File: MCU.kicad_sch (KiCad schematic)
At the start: 50 parts, among them U1901 ADG1607xCP, U1902 ADG1607xCP, U1903 LP38690SDX-3.3/NOPB, U1904 MSP430FR5969IRGZR, U1905 MSP430FR5969IRGZR, U1906 TCAN4551RGYRQ1

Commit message: wired channel alerts; added schematic for test pbc
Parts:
- removed TP1907, TP1908: ~, TestPoint:TestPoint_Pad_1.0x1.0mm, symbol Connector:TestPoint_Small
- added TP? (x2): ~, TestPoint:TestPoint_Pad_1.0x1.0mm, symbol Connector:TestPoint_Small
- renumbered C1911 to C?, C1904 to C?, C1915 to C?, C1905 to C?, C1909 to C?, C1903 to C?, C1912 to C?, C1901 to C?, C1906 to C?, C1907 to C?, C1914 to C?, C1902 to C?, C1910 to C?, C1913 to C?, R1904 to R?, R1906 to R?, R1901 to R?, R1902 to R?, R1903 to R?, R1908 to R?, R1909 to R?, R1907 to R?, TP1911 to TP?, TP1910 to TP?, TP1913 to TP?, TP1916 to TP?, TP1909 to TP?, TP1901 to TP?, TP1903 to TP?, TP1904 to TP?, TP1920 to TP?, TP1915 to TP?, TP1917 to TP?, TP1905 to TP?, TP1918 to TP?, TP1912 to TP?, TP1902 to TP?, TP1906 to TP?, TP1914 to TP?, U1906 to U?, U1902 to U?, U1905 to U?
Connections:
- net 5V_DCDC_1/VOUT: now also TP?.1
- net Ch_EN_7x: now also U?.3 (P1.2/TA1.1/TA0CLK/COUT/A2/C2); no longer U?.42 (PJ.6/HFXIN)
- net Ch_EN_8x: now also U?.9 (P1.3/TA1.2/UCB0STE/A3/C3); no longer U?.43 (PJ.7/HFXOUT)
- net MCU_3V3: now also TP?.1
- net Ch_AL_9: now reaches U?.1 (P1.0/TA0.1/DMAE0/RTCCLK/A0/C0/VREF-/VEREF-)
- net Ch_AL_1: now reaches U?.12 (PJ.0/TDO/TB0OUTH/SMCLK/SRSCG1/C6)
- net Ch_AL_2: now reaches U?.13 (PJ.1/TDI/TCLK/MCLK/SRSCG0/C7)
- net Ch_AL_3: now reaches U?.14 (PJ.2/TMS/ACLK/SROSCOFF/C8)
- net Ch_AL_4: now reaches U?.15 (PJ.3/TCK/SRCPUOFF/C9)
- net Ch_AL_10: now reaches U?.2 (P1.1/TA0.2/TA1CLK/COUT/A1/C1/VREF+/VEREF+)
- net Ch_AL_5: now reaches U?.45 (PJ.4/LFXIN)
- net Ch_AL_6: now reaches U?.46 (PJ.5/LFXOUT)
- net VMEAS_BATT_1: no longer names the net of U?.17 (S1A)
- net VMEAS_BATT_2: no longer names the net of U?.18 (S2A)
- new net Ch_AL_7: U?.42 (PJ.6/HFXIN)
- new net Ch_AL_8: U?.43 (PJ.7/HFXOUT)
- no-connect marks 2 -> 4

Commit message: reduced number of DCDC converter for PV panels; updated test pcb
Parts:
- gave numbers to parts that had none: 44
- renumbered C1908 to C1808, R1905 to R1805, TP1919 to TP1819, U1901 to U1801, U1903 to U1803, U1904 to U1804
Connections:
- net 5V_DCDC_1/VOUT renamed +5V

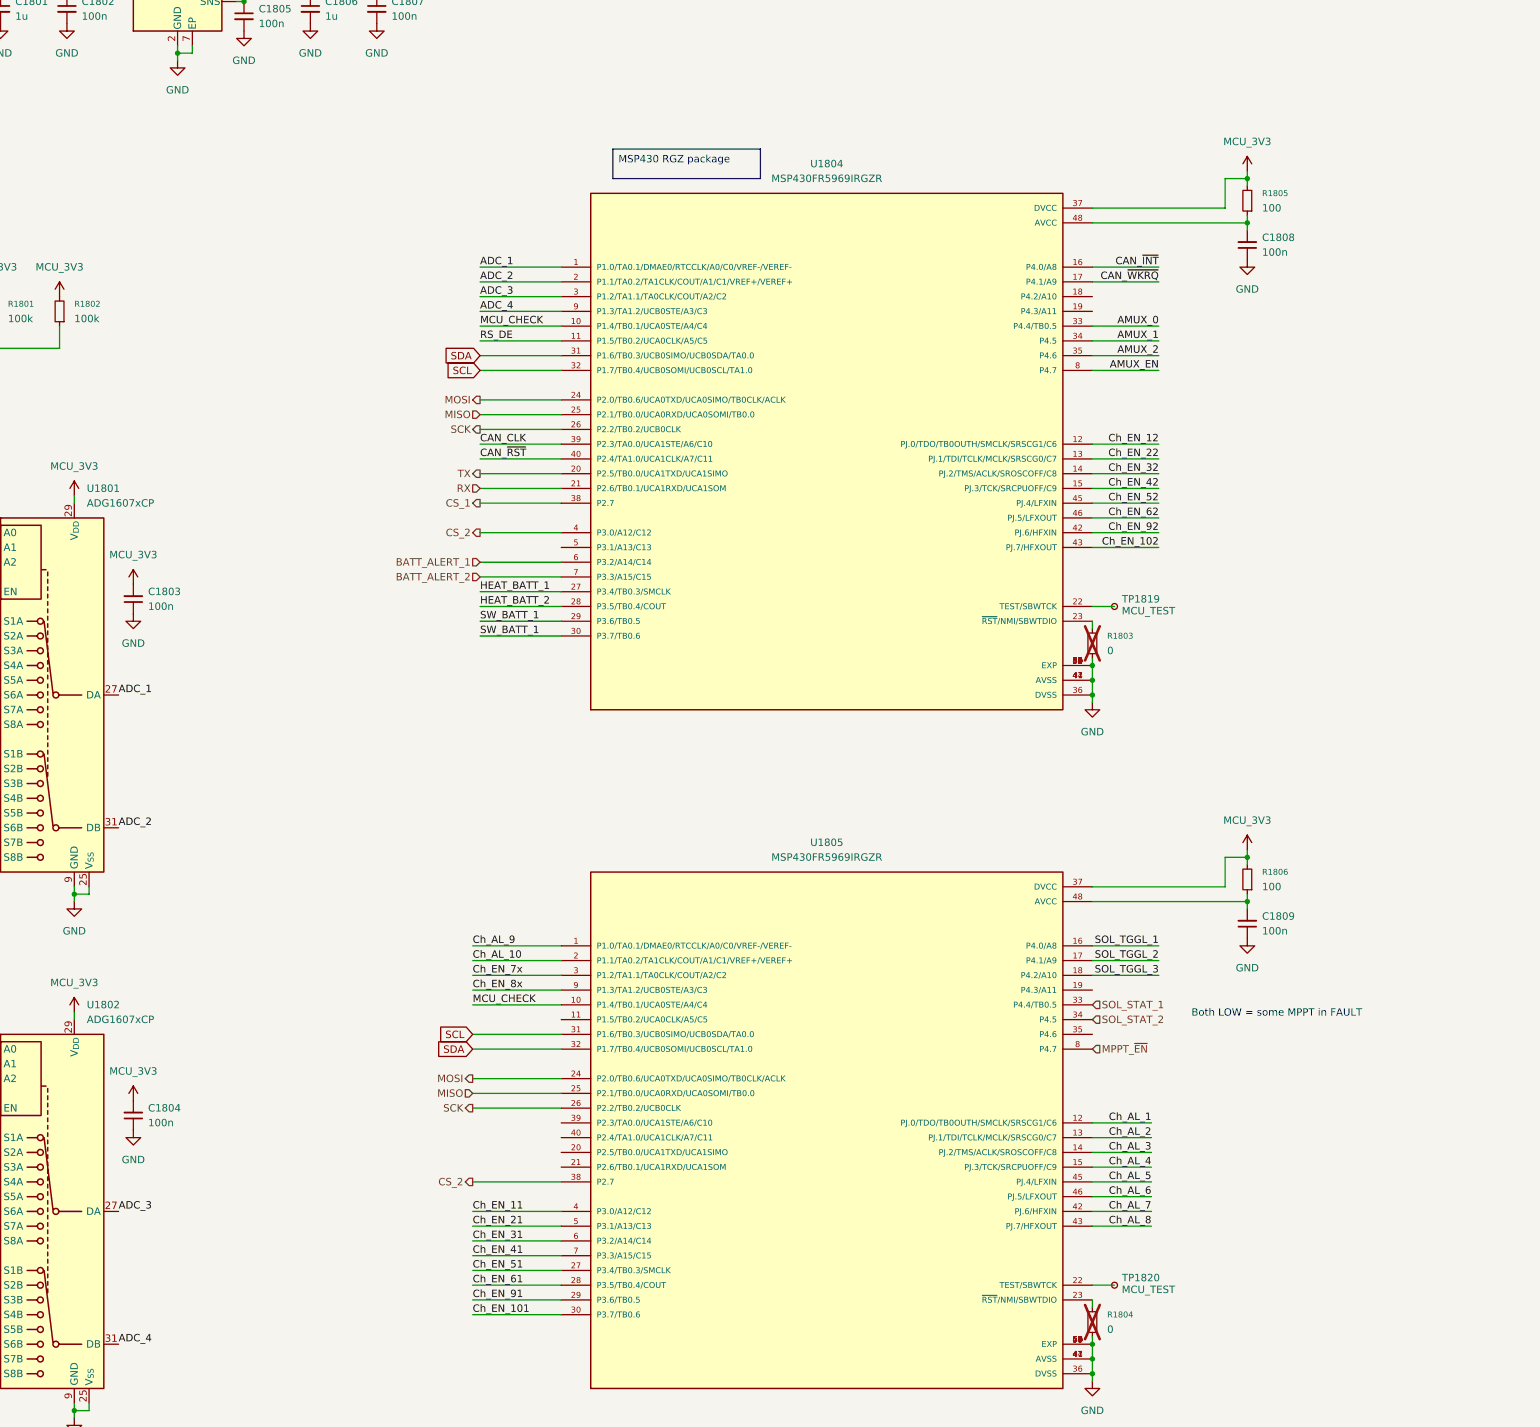
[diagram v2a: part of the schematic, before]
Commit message: added missing heater connectors
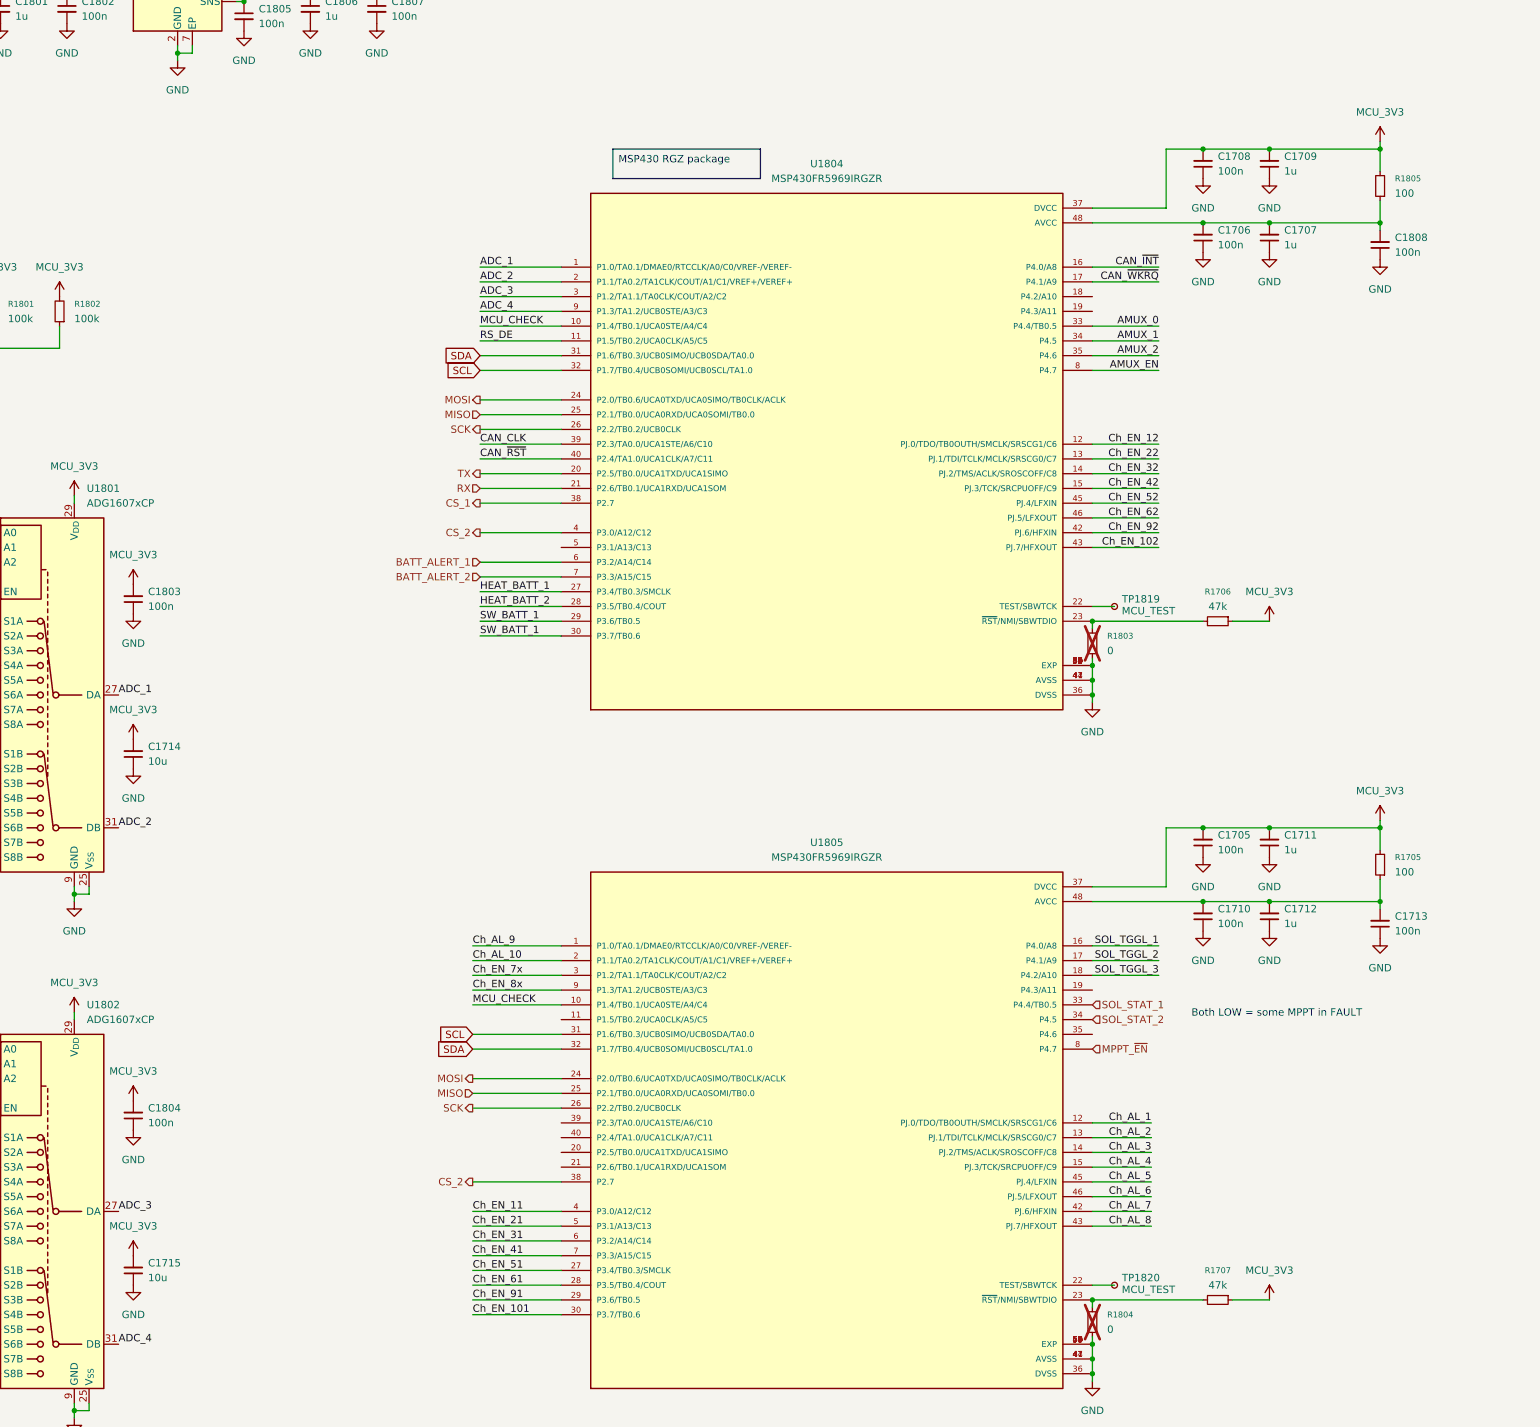
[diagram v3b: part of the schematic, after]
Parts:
- removed C1809: 100n, Capacitor_SMD:C_0603_1608Metric_Pad1.08x0.95mm_HandSolder, symbol Device:C_Small
- removed R1806: 100, Resistor_SMD:R_0603_1608Metric_Pad0.98x0.95mm_HandSolder, symbol Device:R_Small
- added C1705, C1706, C1708, C1710, C1713: 100n, Capacitor_SMD:C_0603_1608Metric_Pad1.08x0.95mm_HandSolder, symbol Device:C_Small
- added C1707, C1709, C1711, C1712: 1u, Capacitor_SMD:C_0603_1608Metric_Pad1.08x0.95mm_HandSolder, symbol Device:C_Small
- added C1714, C1715: 10u, Capacitor_SMD:C_0603_1608Metric_Pad1.08x0.95mm_HandSolder, symbol Device:C_Small
- added R1705: 100, Resistor_SMD:R_0603_1608Metric_Pad0.98x0.95mm_HandSolder, symbol Device:R_Small
- added R1706, R1707: 47k, Resistor_SMD:R_0603_1608Metric_Pad0.98x0.95mm_HandSolder, symbol Device:R_Small
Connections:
- net GND: now also C1705.1, C1706.1, C1707.1, C1708.1, C1709.1, C1710.1, C1711.1, C1712.1, C1713.1, C1714.1, C1715.1
- net MCU_3V3: now also C1705.2, C1708.2, C1709.2, C1711.2, C1714.2, C1715.2, R1705.2, R1706.1, R1707.1
- net at C1808.2, R1805.1, U1804.48 (AVCC): now also C1706.2, C1707.2
- net at R1804.2, U1805.23 (~{RST}/NMI/SBWTDIO): now also R1707.2
- net at U1805.48 (AVCC): now also C1710.2, C1712.2, C1713.2, R1705.1
- net at R1803.2, U1804.23 (~{RST}/NMI/SBWTDIO): now also R1706.2
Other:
- moved on the sheet: C1808, R1805

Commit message: restructurization of the entire project improved
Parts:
- removed C1706, C1708, C1713, C1802, C1805, C1807, C1810, C1814: 100n, Capacitor_SMD:C_0603_1608Metric_Pad1.08x0.95mm_HandSolder, symbol Device:C_Small
- removed C1707, C1712, C1806: 1u, Capacitor_SMD:C_0603_1608Metric_Pad1.08x0.95mm_HandSolder, symbol Device:C_Small
- removed C1714, C1715: 10u, Capacitor_SMD:C_0603_1608Metric_Pad1.08x0.95mm_HandSolder, symbol Device:C_Small
- removed C1813: 330n, Capacitor_SMD:C_0603_1608Metric_Pad1.08x0.95mm_HandSolder, symbol Device:C_Small
- removed R1705, R1807: 100, Resistor_SMD:R_0603_1608Metric_Pad0.98x0.95mm_HandSolder, symbol Device:R_Small
- removed R1706: 47k, Resistor_SMD:R_0603_1608Metric_Pad0.98x0.95mm_HandSolder, symbol Device:R_Small
- removed R1802: 100k, Resistor_SMD:R_0603_1608Metric_Pad0.98x0.95mm_HandSolder, symbol Device:R_Small
- removed R1808: 33k, Resistor_SMD:R_0603_1608Metric_Pad0.98x0.95mm_HandSolder, symbol Device:R_Small
- removed TP1805, TP1807, TP1808, TP1809, TP1810, TP1811, TP1812, TP1815, TP1816, TP1817, TP1818, TP1819, TP1820: ~, TestPoint:TestPoint_Pad_1.0x1.0mm, symbol Connector:TestPoint_Small
- removed U1803: LP38690SDX-3.3/NOPB, Package_SON:WSON-6-1EP_3x3mm_P0.95mm, symbol Regulator_Linear:LP38691SD-3.3
- removed U1804, U1805: MSP430FR5969IRGZR, Package_DFN_QFN:Texas_RGZ0048A_VQFN-48-1EP_7x7mm_P0.5mm_EP5.15x5.15mm_ThermalVias, symbol MSP430FR5969IRGZR:MSP430FR5969IRGZR
- added C5002, C5007, C5009, C5013, C5014, C5022, C5023, C5027: 100n, Capacitor_SMD:C_0603_1608Metric_Pad1.08x0.95mm_HandSolder, symbol Device:C_Small
- added C5004, C5006: 10u, Capacitor_SMD:C_0603_1608Metric_Pad1.08x0.95mm_HandSolder, symbol Device:C_Small
- added C5008, C5018, C5020: 1u, Capacitor_SMD:C_0603_1608Metric_Pad1.08x0.95mm_HandSolder, symbol Device:C_Small
- added C5010, C5011, C5012: 1n, Capacitor_SMD:C_0603_1608Metric_Pad1.08x0.95mm_HandSolder, symbol Device:C_Small
- added C5026: 330n, Capacitor_SMD:C_0603_1608Metric_Pad1.08x0.95mm_HandSolder, symbol Device:C_Small
- added J5001, J5002, J5003, J5004: JTAG, symbol Connector:Conn_01x04_Socket
- added R5002, R5003, R5004, R5005, R5006, R5007, R5008, R5009, R5010, R5011, R5012: 100k, Resistor_SMD:R_0603_1608Metric_Pad0.98x0.95mm_HandSolder, symbol Device:R_Small
- added R5015, R5017: 47k, Resistor_SMD:R_0603_1608Metric_Pad0.98x0.95mm_HandSolder, symbol Device:R_Small
- added R5019, R5020: 100, Resistor_SMD:R_0603_1608Metric_Pad0.98x0.95mm_HandSolder, symbol Device:R_Small
- added R5021: 33k, Resistor_SMD:R_0603_1608Metric_Pad0.98x0.95mm_HandSolder, symbol Device:R_Small
- added R_MISO_5001, R_MOSI_5001, R_RX_5001, R_TX_5001: 0, Resistor_SMD:R_0603_1608Metric_Pad0.98x0.95mm_HandSolder, symbol Device:R_Small
- added TP5001, TP5002, TP5007: ~, TestPoint:TestPoint_Pad_1.0x1.0mm, symbol Connector:TestPoint_Small
- added U5003: LP38690SDX-3.3/NOPB, Package_SON:WSON-6-1EP_3x3mm_P0.95mm, symbol Regulator_Linear:LP38691SD-3.3
- added U5004, U5005: MSP430FR5969IRGZR, Package_DFN_QFN:Texas_RGZ0048A_VQFN-48-1EP_7x7mm_P0.5mm_EP5.15x5.15mm_ThermalVias, symbol MSP430FR5969IRGZR:MSP430FR5969IRGZR
- renumbered C1801 to C5001, C1803 to C5003, C1804 to C5005, C1705 to C5015, C1710 to C5016, C1709 to C5017, C1711 to C5019, C1808 to C5021, C1811 to C5024, C1812 to C5025, C1815 to C5028, R1801 to R5001, R1803 to R5013, R1804 to R5014, R1707 to R5016, R1805 to R5018, R1809 to R5022, TP1801 to TP5003, TP1802 to TP5004, TP1803 to TP5005, TP1804 to TP5006, TP1806 to TP5008, TP1813 to TP5009, TP1814 to TP5010, U1801 to U5001, U1802 to U5002, U1806 to U5006
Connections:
- net TMEAS_SOL_1 is gone; now on net AMEAS_6: U5001.22 (S6A)
- net TMEAS_SOL_2 is gone; now on net AMEAS_7: U5001.23 (S7A)
- net TMEAS_SOL_3 is gone; now on net AMEAS_8: U5001.24 (S8A)
- net +5V: now also C5002.1, TP5001.1, U5003.1 (IN), U5003.6 (IN)
- net ADC_1: now also U5004.1 (P1.0/TA0.1/DMAE0/RTCCLK/A0/C0/VREF-/VEREF-)
- net ADC_2: now also U5004.2 (P1.1/TA0.2/TA1CLK/COUT/A1/C1/VREF+/VEREF+)
- net ADC_3: now also U5004.3 (P1.2/TA1.1/TA0CLK/COUT/A2/C2)
- net ADC_4: now also U5004.9 (P1.3/TA1.2/UCB0STE/A3/C3)
- net AMEAS_1: now also U5001.17 (S1A); no longer U5001.8 (S1B)
- net AMEAS_10: now also U5001.7 (S2B); no longer U5001.20 (S4A)
- net AMEAS_2: now also U5001.18 (S2A); no longer U5001.7 (S2B)
- net AMEAS_3: now also U5001.19 (S3A); no longer U5001.6 (S3B)
- net AMEAS_4: now also U5001.20 (S4A); no longer U5001.5 (S4B)
- net AMEAS_5: now also U5001.21 (S5A); no longer U5001.4 (S5B)
- net AMEAS_6: no longer U5001.3 (S6B)
- net AMEAS_7: no longer U5001.17 (S1A)
- net AMEAS_8: no longer U5001.18 (S2A)
- net AMEAS_9: now also U5001.8 (S1B); no longer U5001.19 (S3A)
- net AMEAS_BUS: now also U5004.10 (P1.4/TB0.1/UCA0STE/A4/C4); no longer U5001.21 (S5A)
- net AMUX_0: now also U5004.33 (P4.4/TB0.5)
- net AMUX_1: now also U5004.34 (P4.5)
- net AMUX_2: now also U5004.35 (P4.6)
- net AMUX_EN: now also U5004.8 (P4.7)
- net BATT_ALERT_1: now also U5004.6 (P3.2/A14/C14)
- net BATT_ALERT_2: now also U5004.7 (P3.3/A15/C15)
- net CAN_CLK: now also U5004.40 (P2.4/TA1.0/UCA1CLK/A7/C11), U5005.40 (P2.4/TA1.0/UCA1CLK/A7/C11)
- net CAN_H: now also R5020.1
- net CAN_L: now also R5020.2
- net CAN_~{INT}: now also U5004.16 (P4.0/A8)
- net CAN_~{RST}: now also U5004.39 (P2.3/TA0.0/UCA1STE/A6/C10), U5005.39 (P2.3/TA0.0/UCA1STE/A6/C10)
- net CAN_~{WKRQ}: now also U5004.17 (P4.1/A9)
- net CS_1: now also U5004.38 (P2.7), U5005.11 (P1.5/TB0.2/UCA0CLK/A5/C5)
- net CS_2: now also U5004.4 (P3.0/A12/C12), U5005.38 (P2.7)
- net Ch_AL_1: now also R5002.2, U5005.12 (PJ.0/TDO/TB0OUTH/SMCLK/SRSCG1/C6)
- net Ch_AL_10: now also R5005.2, U5005.2 (P1.1/TA0.2/TA1CLK/COUT/A1/C1/VREF+/VEREF+)
- net Ch_AL_2: now also R5007.2, U5005.13 (PJ.1/TDI/TCLK/MCLK/SRSCG0/C7)
- net Ch_AL_3: now also R5010.2, U5005.14 (PJ.2/TMS/ACLK/SROSCOFF/C8)
- net Ch_AL_4: now also R5003.2, U5005.15 (PJ.3/TCK/SRCPUOFF/C9)
- net Ch_AL_5: now also R5008.2, U5005.45 (PJ.4/LFXIN)
- net Ch_AL_6: now also R5011.2, U5005.46 (PJ.5/LFXOUT)
- net Ch_AL_7: now also R5004.2, U5005.42 (PJ.6/HFXIN)
- net Ch_AL_8: now also R5009.2, U5005.43 (PJ.7/HFXOUT)
- net Ch_AL_9: now also R5012.2, U5005.1 (P1.0/TA0.1/DMAE0/RTCCLK/A0/C0/VREF-/VEREF-)
- net Ch_EN_101: now also U5005.30 (P3.7/TB0.6)
- net Ch_EN_102: now also U5004.43 (PJ.7/HFXOUT)
- net Ch_EN_11: now also U5005.4 (P3.0/A12/C12)
- net Ch_EN_12: now also U5004.12 (PJ.0/TDO/TB0OUTH/SMCLK/SRSCG1/C6)
- net Ch_EN_21: now also U5005.5 (P3.1/A13/C13)
- net Ch_EN_22: now also U5004.13 (PJ.1/TDI/TCLK/MCLK/SRSCG0/C7)
- net Ch_EN_31: now also U5005.6 (P3.2/A14/C14)
- net Ch_EN_32: now also U5004.14 (PJ.2/TMS/ACLK/SROSCOFF/C8)
- net Ch_EN_41: now also U5005.7 (P3.3/A15/C15)
- net Ch_EN_42: now also U5004.15 (PJ.3/TCK/SRCPUOFF/C9)
- net Ch_EN_51: now also U5005.27 (P3.4/TB0.3/SMCLK)
- net Ch_EN_52: now also U5004.45 (PJ.4/LFXIN)
- net Ch_EN_61: now also U5005.28 (P3.5/TB0.4/COUT)
- net Ch_EN_62: now also U5004.46 (PJ.5/LFXOUT)
- net Ch_EN_7x: now also U5004.29 (P3.6/TB0.5)
- net Ch_EN_8x: now also U5004.30 (P3.7/TB0.6)
- net Ch_EN_91: now also U5005.29 (P3.6/TB0.5)
- net Ch_EN_92: now also U5004.42 (PJ.6/HFXIN)
- net GND: now also C5002.2, C5004.1, C5006.1, C5007.2, C5008.2, C5009.2, C5010.1, C5011.1, C5012.1, C5013.1, C5014.1, C5018.1, C5020.1, C5022.1, C5023.1, C5026.1, C5027.1, J5001.4 (Pin_4), J5002.4 (Pin_4), J5003.4 (Pin_4), J5004.4 (Pin_4), U5003.2 (GND), U5003.7 (EP), U5004.36 (DVSS), U5004.41 (AVSS), U5004.44 (AVSS), U5004.47 (AVSS), U5004.49 (EXP), U5004.50 (EXP), U5004.51 (EXP), U5004.52 (EXP), U5004.53 (EXP), U5004.54 (EXP), U5004.55 (EXP), U5004.56 (EXP), U5004.57 (EXP), U5004.58 (EXP), U5004.59 (EXP), U5004.60 (EXP), U5004.61 (EXP), U5005.36 (DVSS), U5005.41 (AVSS), U5005.44 (AVSS), U5005.47 (AVSS), U5005.49 (EXP), U5005.50 (EXP), U5005.51 (EXP), U5005.52 (EXP), U5005.53 (EXP), U5005.54 (EXP), U5005.55 (EXP), U5005.56 (EXP), U5005.57 (EXP), U5005.58 (EXP), U5005.59 (EXP), U5005.60 (EXP), U5005.61 (EXP)
- net HEAT_BATT_1: now also U5004.19 (P4.3/A11)
- net HEAT_BATT_2: now also U5004.18 (P4.2/A10)
- net MCU_3V3: now also C5004.2, C5006.2, C5007.1, C5008.1, C5009.1, C5013.2, C5023.2, C5027.2, J5001.1 (Pin_1), J5002.1 (Pin_1), J5003.1 (Pin_1), J5004.1 (Pin_1), R5002.1, R5003.1, R5004.1, R5005.1, R5006.1, R5007.1, R5008.1, R5009.1, R5010.1, R5011.1, R5012.1, R5015.1, R5017.1, R5019.2, TP5002.1, U5003.4 (OUT), U5003.5 (SNS), U5004.37 (DVCC), U5005.37 (DVCC); no longer U5006.15 (INH)
- net MISO: now also R_MOSI_5001.2, U5004.25 (P2.1/TB0.0/UCA0RXD/UCA0SOMI/TB0.0)
- net MOSI: now also R_MISO_5001.1, U5004.24 (P2.0/TB0.6/UCA0TXD/UCA0SIMO/TB0CLK/ACLK)
- net MPPT_~{EN}: now also U5004.5 (P3.1/A13/C13)
- net RX: now also R_RX_5001.1, U5005.21 (P2.6/TB0.1/UCA1RXD/UCA1SOM)
- net SCK: now also U5004.26 (P2.2/TB0.2/UCB0CLK), U5005.26 (P2.2/TB0.2/UCB0CLK)
- net SCL: now also R5006.2, U5004.32 (P1.7/TB0.4/UCB0SOMI/UCB0SCL/TA1.0), U5005.31 (P1.6/TB0.3/UCB0SIMO/UCB0SDA/TA0.0)
- net SDA: now also U5004.31 (P1.6/TB0.3/UCB0SIMO/UCB0SDA/TA0.0), U5005.32 (P1.7/TB0.4/UCB0SOMI/UCB0SCL/TA1.0)
- net SOL_STAT_1: now also U5005.35 (P4.6)
- net SOL_STAT_2: now also U5005.8 (P4.7)
- net TX: now also R_TX_5001.2, U5005.20 (P2.5/TB0.0/UCA1TXD/UCA1SIMO)
- net VMEAS_SOL_5: now also TP5007.1
- net at C5021.2, R5018.1: now also C5014.2, C5018.2, U5004.48 (AVCC)
- net at R5014.2, R5016.2: now also C5010.2, C5011.2, J5003.3 (Pin_3), J5004.3 (Pin_3), R5015.2, U5005.23 (~{RST}/NMI/SBWTDIO)
- net at R5013.2: now also C5012.2, J5001.3 (Pin_3), J5002.3 (Pin_3), R5017.2, U5004.23 (~{RST}/NMI/SBWTDIO)
- net at U5006.18 (FLTR): now also C5026.2
- net at C5028.2, R5022.2: now also R5021.1
- net at U5006.12 (WAKE): now also R5021.2
- net at C5016.2: now also C5020.2, C5022.2, R5019.1, U5005.48 (AVCC)
- net Ch_V_7: now reaches U5002.17 (S1A)
- net Ch_V_8: now reaches U5002.18 (S2A)
- net AMEAS_BATT_1 renamed Ch_V_5
- net AMEAS_BATT_2 renamed Ch_V_6
- new net: R_TX_5001.1, U5004.20 (P2.5/TB0.0/UCA1TXD/UCA1SIMO)
- new net: J5001.2 (Pin_2), J5002.2 (Pin_2), U5004.22 (TEST/SBWTCK)
- new net: J5003.2 (Pin_2), J5004.2 (Pin_2), U5005.22 (TEST/SBWTCK)
- new net: R_MOSI_5001.1, U5005.24 (P2.0/TB0.6/UCA0TXD/UCA0SIMO/TB0CLK/ACLK)
- new net: R_MISO_5001.2, U5005.25 (P2.1/TB0.0/UCA0RXD/UCA0SOMI/TB0.0)
- new net: R_RX_5001.2, U5004.21 (P2.6/TB0.1/UCA1RXD/UCA1SOM)
- new net Ch_V_1: U5001.6 (S3B)
- new net Ch_V_2: U5001.5 (S4B)
- new net Ch_V_3: U5001.4 (S5B)
- new net Ch_V_4: U5001.3 (S6B)
- new net RS_DIR: U5004.11 (P1.5/TB0.2/UCA0CLK/A5/C5)
- new net SOL_EN_1: U5005.16 (P4.0/A8)
- new net SOL_EN_2: U5005.17 (P4.1/A9)
- new net SOL_EN_3: U5005.18 (P4.2/A10)
- new net SOL_EN_4: U5005.19 (P4.3/A11)
- new net SOL_EN_5: U5005.33 (P4.4/TB0.5)
- new net SOL_EN_6: U5005.34 (P4.5)
- new net SW_BATT_11: U5004.27 (P3.4/TB0.3/SMCLK)
- new net SW_BATT_12: U5005.9 (P1.3/TA1.2/UCB0STE/A3/C3)
- new net SW_BATT_21: U5004.28 (P3.5/TB0.4/COUT)
- new net SW_BATT_22: U5005.3 (P1.2/TA1.1/TA0CLK/COUT/A2/C2)
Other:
- sheet RS422_485 ports: added Input, UART_DIR; removed POWER, UART_DE
- note added: "Pull downs on device side"
- note added: "Pull up on MCU side"
- note removed: "Both LOW = some MPPT in FAULT"
- moved on the sheet: C5015, C5016, C5017, C5019, C5021, C5024, C5025, C5028, R5001, R5013, R5014, R5016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

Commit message: added universal switch, added simples current source, reworked test schematic and pcb
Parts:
- removed C5010: 1n, Capacitor_SMD:C_0603_1608Metric_Pad1.08x0.95mm_HandSolder, symbol Device:C_Small
- removed J5001, J5003: JTAG, symbol Connector:Conn_01x04_Socket
- removed R5015: 47k, Resistor_SMD:R_0603_1608Metric_Pad0.98x0.95mm_HandSolder, symbol Device:R_Small
- added J1301: Conn_01x02_Pin, Connector_PinHeader_2.54mm:PinHeader_1x02_P2.54mm_Vertical, symbol Connector:Conn_01x02_Pin
- added TP1302, TP1303, TP1304, TP1305, TP1315, TP1316, TP1317, TP1318: ~, TestPoint:TestPoint_Pad_1.0x1.0mm, symbol Connector:TestPoint_Small
- C1305: renamed from C5005; now not fitted; now left out of the parts list
- C1306: renamed from C5006; now not fitted; now left out of the parts list
- J1302: renamed from J5002; footprint (none) -> Connector_PinSocket_2.54mm:PinSocket_1x04_P2.54mm_Vertical
- J1303: renamed from J5004; footprint (none) -> Connector_PinSocket_2.54mm:PinSocket_1x04_P2.54mm_Vertical
- R1302: renamed from R5003; now not fitted; now left out of the parts list
- R1303: renamed from R5004; now not fitted; now left out of the parts list
- R1304: renamed from R5005; now not fitted; now left out of the parts list
- R1306: renamed from R5007; now not fitted; now left out of the parts list
- R1307: renamed from R5008; now not fitted; now left out of the parts list
- R1308: renamed from R5009; now not fitted; now left out of the parts list
- R1310: renamed from R5010; now not fitted; now left out of the parts list
- R1311: renamed from R5011; now not fitted; now left out of the parts list
- R1312: renamed from R5012; now not fitted; now left out of the parts list
- U1302: renamed from U5002; now not fitted; now left out of the parts list
- renumbered C5001 to C1301, C5002 to C1302, C5003 to C1303, C5004 to C1304, C5007 to C1307, C5008 to C1308, C5009 to C1309, C5011 to C1310, C5012 to C1311, C5013 to C1312, C5014 to C1313, C5015 to C1314, C5016 to C1315, C5017 to C1316, C5018 to C1317, C5019 to C1318, C5020 to C1319, C5021 to C1320, C5022 to C1321, C5023 to C1322, C5024 to C1323, C5025 to C1324, C5026 to C1325, C5027 to C1326, C5028 to C1327, R5002 to R1301, R5001 to R1305, R5006 to R1309, R5013 to R1313, R5014 to R1314, R5016 to R1315, R5017 to R1316, R5018 to R1317, R5019 to R1318, R5020 to R1319, R5021 to R1320, R5022 to R1321, R_MISO_5001 to R_MISO_1301, R_MOSI_5001 to R_MOSI_1301, R_RX_5001 to R_RX_1301, R_TX_5001 to R_TX_1301, TP5001 to TP1301, TP5002 to TP1306, TP5003 to TP1307, TP5004 to TP1308, TP5005 to TP1309, TP5006 to TP1310, TP5007 to TP1311, TP5008 to TP1312, TP5009 to TP1313, TP5010 to TP1314, U5001 to U1301, U5003 to U1303, U5004 to U1304, U5005 to U1305, U5006 to U1306
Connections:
- net TMEAS_BATT_1 is gone; now on net AMEAS_9: TP1313.1, U1302.8 (S1B)
- net VMEAS_SOL_1 is gone; now on net AMEAS_2: TP1307.1, U1302.19 (S3A)
- net ADC_1: now also U1301.31 (DB), TP1303.1; no longer U1301.27 (DA)
- net ADC_2: now also U1301.27 (DA), TP1302.1; no longer U1301.31 (DB)
- net ADC_3: now also TP1304.1
- net ADC_4: now also TP1305.1
- net AMEAS_BUS: now also U1304.4 (P3.0/A12/C12); no longer U1304.10 (P1.4/TB0.1/UCA0STE/A4/C4)
- net AMUX_EN: now also U1304.39 (P2.3/TA0.0/UCA1STE/A6/C10); no longer U1304.8 (P4.7)
- net CAN_CLK: now also TP1318.1
- net CAN_~{INT}: now also TP1315.1
- net CAN_~{RST}: now also U1304.26 (P2.2/TB0.2/UCB0CLK), U1305.26 (P2.2/TB0.2/UCB0CLK), TP1317.1; no longer U1304.39 (P2.3/TA0.0/UCA1STE/A6/C10), U1305.39 (P2.3/TA0.0/UCA1STE/A6/C10)
- net CAN_~{WKRQ}: now also TP1316.1
- net CS_1: now also U1304.10 (P1.4/TB0.1/UCA0STE/A4/C4), U1305.10 (P1.4/TB0.1/UCA0STE/A4/C4); no longer U1304.38 (P2.7), U1305.11 (P1.5/TB0.2/UCA0CLK/A5/C5)
- net CS_2: now also U1304.38 (P2.7); no longer U1304.4 (P3.0/A12/C12)
- net MCU_3V3: now also J1301.1 (Pin_1); no longer C1307.1, C1308.1, C1309.1, TP1306.1, U1303.4 (OUT), U1303.5 (SNS)
- net RS_DIR: now also U1305.39 (P2.3/TA0.0/UCA1STE/A6/C10); no longer U1304.11 (P1.5/TB0.2/UCA0CLK/A5/C5)
- net SCK: now also U1304.11 (P1.5/TB0.2/UCA0CLK/A5/C5), U1305.11 (P1.5/TB0.2/UCA0CLK/A5/C5); no longer U1304.26 (P2.2/TB0.2/UCB0CLK), U1305.26 (P2.2/TB0.2/UCB0CLK)
- net SCL: now also U1305.32 (P1.7/TB0.4/UCB0SOMI/UCB0SCL/TA1.0); no longer U1305.31 (P1.6/TB0.3/UCB0SIMO/UCB0SDA/TA0.0)
- net SDA: now also U1305.31 (P1.6/TB0.3/UCB0SIMO/UCB0SDA/TA0.0); no longer U1305.32 (P1.7/TB0.4/UCB0SOMI/UCB0SCL/TA1.0)
- new net: C1307.1, C1308.1, C1309.1, J1301.2 (Pin_2), TP1306.1, U1303.4 (OUT), U1303.5 (SNS)
- no-connect marks 4 -> 3
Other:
- note added: "Used in test"
- note added: "kouknout jak na odpory analog vstupu a jak nastavit odporove delice pro mereni napeti"
- moved on the sheet: C1303, C1304, R1301, R1305, R1309, U1301
